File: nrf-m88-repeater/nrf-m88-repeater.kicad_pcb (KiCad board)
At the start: 2 copper layers, 14 parts, among them J1 Conn_02x03_Counter_Clockwise, SW1 SW_Push, U1 ATmega88-20P, U2 NRF24L01_Breakout, U3 LP2950-3.3_TO92

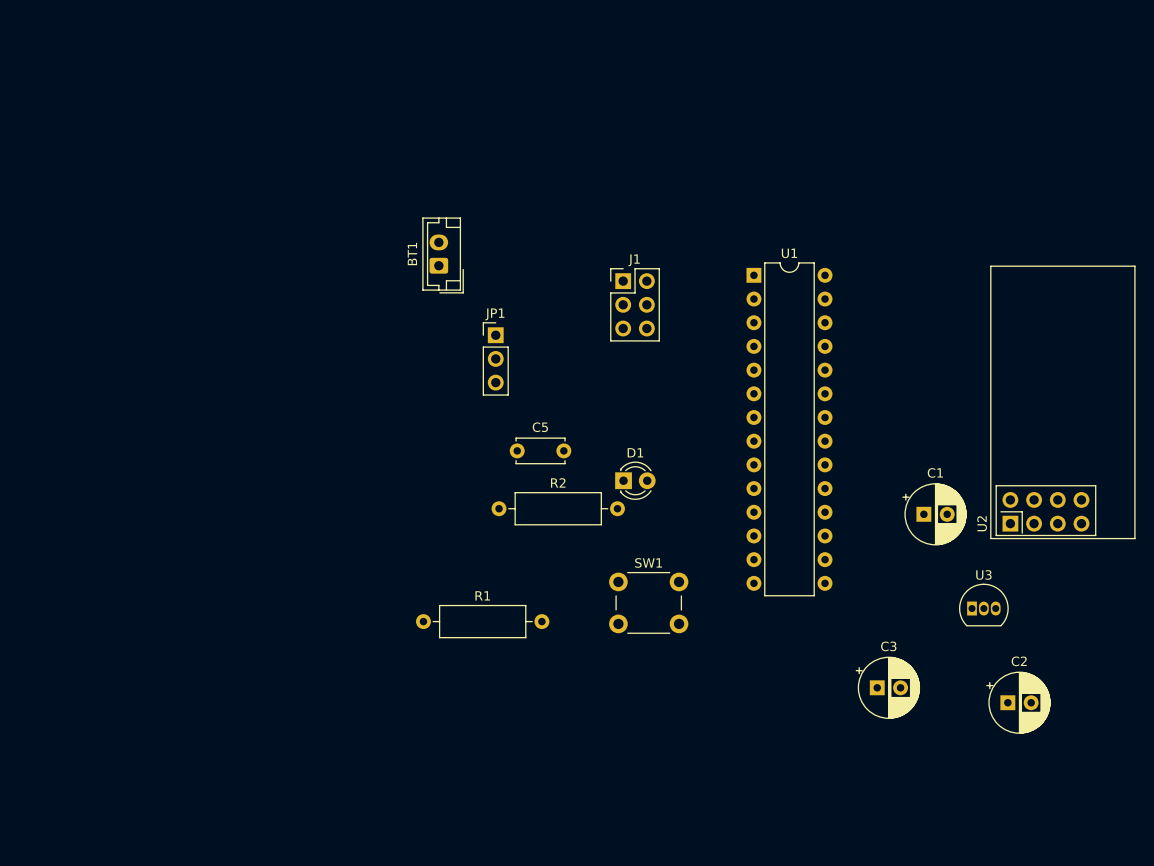
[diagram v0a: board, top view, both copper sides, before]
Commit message: Updated Generic KiCad Model
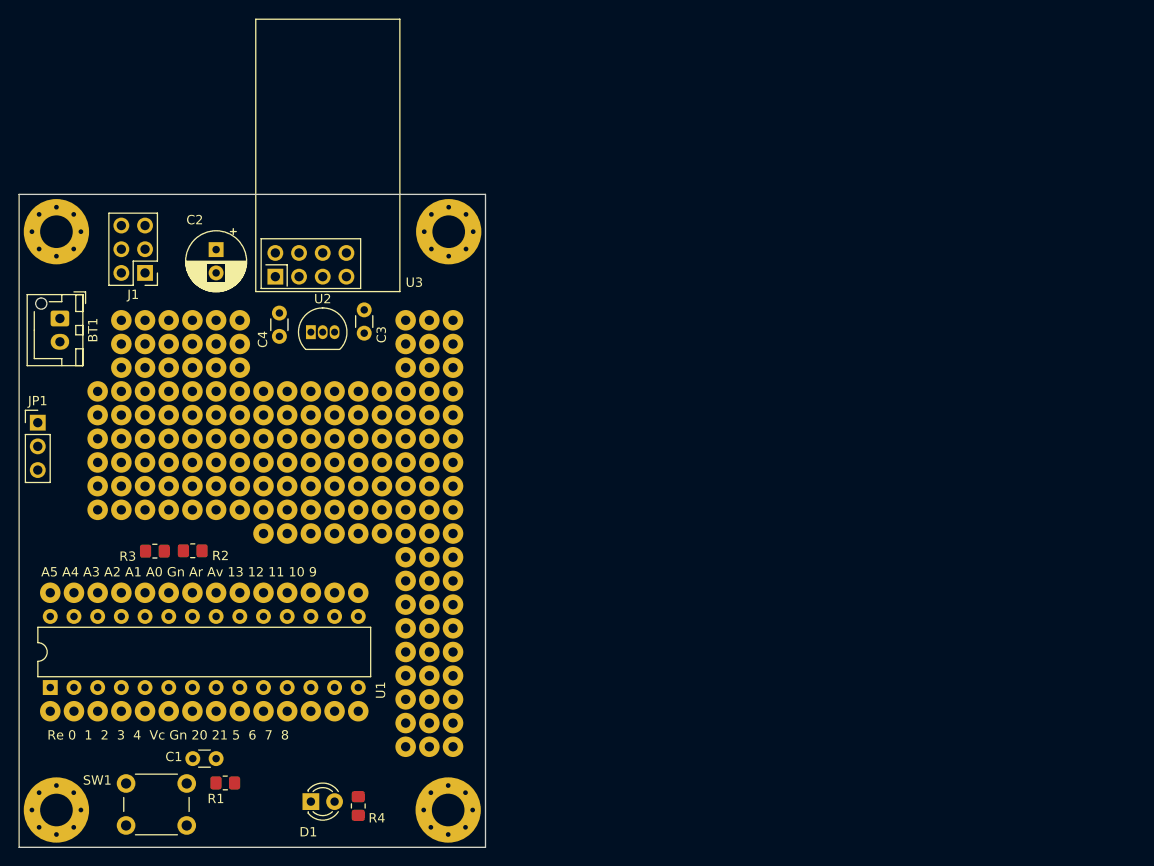
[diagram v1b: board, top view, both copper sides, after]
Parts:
- removed the C2 at (156.0, 104.5)
- removed C5: 100n, Capacitor_THT:C_Disc_D5.0mm_W2.5mm_P5.00mm
- added C1: 100n, Capacitor_THT:C_Disc_D3.0mm_W1.6mm_P2.50mm, F.Cu at (68.6, 110.5)
- added C3: 1u, Capacitor_THT:C_Disc_D3.0mm_W1.6mm_P2.50mm, F.Cu at (87.0, 62.4)
- added H1: MountingHole, MountingHole:MountingHole_3.5mm_Pad_Via, F.Cu at (96.1, 54.0)
- added H2: MountingHole, MountingHole:MountingHole_3.5mm_Pad_Via, F.Cu at (54.0, 54.0)
- added H3: MountingHole, MountingHole:MountingHole_3.5mm_Pad_Via, F.Cu at (96.0, 116.0)
- added H4: MountingHole, MountingHole:MountingHole_3.5mm_Pad_Via, F.Cu at (54.0, 116.0)
- added R2: 8.2k, Resistor_SMD:R_0805_2012Metric_Pad1.20x1.40mm_HandSolder, F.Cu at (68.6, 88.2)
- added R3: 2.2k, Resistor_SMD:R_0805_2012Metric_Pad1.20x1.40mm_HandSolder, F.Cu at (64.6, 88.2)
- added REF**: Pad, mikes-feet-library:ProtoPad, F.Cu at (58.4, 73.7)
- added REF**: Pad, mikes-feet-library:ProtoPad, F.Cu at (96.5, 66.0)
- added REF**: Pad, mikes-feet-library:ProtoPad, F.Cu at (91.4, 104.1)
- added REF**: Pad, mikes-feet-library:ProtoPad, F.Cu at (83.8, 76.2)
- added REF**: Pad, mikes-feet-library:ProtoPad, F.Cu at (76.2, 105.4)
- added REF**: Pad, mikes-feet-library:ProtoPad, F.Cu at (73.7, 105.4)
- added REF**: Pad, mikes-feet-library:ProtoPad, F.Cu at (96.5, 101.6)
- added REF**: Pad, mikes-feet-library:ProtoPad, F.Cu at (71.1, 83.8)
- added REF**: Pad, mikes-feet-library:ProtoPad, F.Cu at (73.7, 71.1)
- added REF**: Pad, mikes-feet-library:ProtoPad, F.Cu at (61.0, 92.7)
- added REF**: Pad, mikes-feet-library:ProtoPad, F.Cu at (81.3, 71.1)
- added REF**: Pad, mikes-feet-library:ProtoPad, F.Cu at (81.3, 78.7)
- added REF**: Pad, mikes-feet-library:ProtoPad, F.Cu at (58.4, 81.3)
- added REF**: Pad, mikes-feet-library:ProtoPad, F.Cu at (96.5, 86.4)
- added REF**: Pad, mikes-feet-library:ProtoPad, F.Cu at (61.0, 83.8)
- added REF**: Pad, mikes-feet-library:ProtoPad, F.Cu at (94.0, 66.0)
- added REF**: Pad, mikes-feet-library:ProtoPad, F.Cu at (63.5, 83.8)
- added REF**: Pad, mikes-feet-library:ProtoPad, F.Cu at (86.4, 92.7)
- added REF**: Pad, mikes-feet-library:ProtoPad, F.Cu at (61.0, 81.3)
- added REF**: Pad, mikes-feet-library:ProtoPad, F.Cu at (94.0, 73.7)
- added REF**: Pad, mikes-feet-library:ProtoPad, F.Cu at (73.7, 66.0)
- added REF**: Pad, mikes-feet-library:ProtoPad, F.Cu at (73.7, 68.6)
- added REF**: Pad, mikes-feet-library:ProtoPad, F.Cu at (58.4, 71.1)
- added REF**: Pad, mikes-feet-library:ProtoPad, F.Cu at (73.7, 78.7)
- added REF**: Pad, mikes-feet-library:ProtoPad, F.Cu at (66.0, 73.7)
- added REF**: Pad, mikes-feet-library:ProtoPad, F.Cu at (96.5, 88.9)
- added REF**: Pad, mikes-feet-library:ProtoPad, F.Cu at (91.4, 109.2)
- added REF**: Pad, mikes-feet-library:ProtoPad, F.Cu at (63.5, 78.7)
- added REF**: Pad, mikes-feet-library:ProtoPad, F.Cu at (88.9, 76.2)
- added REF**: Pad, mikes-feet-library:ProtoPad, F.Cu at (81.3, 83.8)
- added REF**: Pad, mikes-feet-library:ProtoPad, F.Cu at (58.4, 76.2)
- added REF**: Pad, mikes-feet-library:ProtoPad, F.Cu at (68.6, 78.7)
- added REF**: Pad, mikes-feet-library:ProtoPad, F.Cu at (94.0, 99.1)
- added REF**: Pad, mikes-feet-library:ProtoPad, F.Cu at (68.6, 66.0)
- added REF**: Pad, mikes-feet-library:ProtoPad, F.Cu at (83.8, 86.4)
- added REF**: Pad, mikes-feet-library:ProtoPad, F.Cu at (78.7, 76.2)
- added REF**: Pad, mikes-feet-library:ProtoPad, F.Cu at (73.7, 63.5)
- added REF**: Pad, mikes-feet-library:ProtoPad, F.Cu at (68.6, 73.7)
- added REF**: Pad, mikes-feet-library:ProtoPad, F.Cu at (63.5, 105.4)
- added REF**: Pad, mikes-feet-library:ProtoPad, F.Cu at (86.4, 81.3)
- added REF**: Pad, mikes-feet-library:ProtoPad, F.Cu at (66.0, 92.7)
- added REF**: Pad, mikes-feet-library:ProtoPad, F.Cu at (53.3, 92.7)
- added REF**: Pad, mikes-feet-library:ProtoPad, F.Cu at (94.0, 68.6)
- added REF**: Pad, mikes-feet-library:ProtoPad, F.Cu at (91.4, 86.4)
- added REF**: Pad, mikes-feet-library:ProtoPad, F.Cu at (96.5, 68.6)
- added REF**: Pad, mikes-feet-library:ProtoPad, F.Cu at (83.8, 105.4)
- added REF**: Pad, mikes-feet-library:ProtoPad, F.Cu at (76.2, 81.3)
- added REF**: Pad, mikes-feet-library:ProtoPad, F.Cu at (94.0, 101.6)
- added REF**: Pad, mikes-feet-library:ProtoPad, F.Cu at (86.4, 78.7)
- added REF**: Pad, mikes-feet-library:ProtoPad, F.Cu at (58.4, 83.8)
- added REF**: Pad, mikes-feet-library:ProtoPad, F.Cu at (55.9, 92.7)
- added REF**: Pad, mikes-feet-library:ProtoPad, F.Cu at (66.0, 63.5)
- added REF**: Pad, mikes-feet-library:ProtoPad, F.Cu at (76.2, 71.1)
- added REF**: Pad, mikes-feet-library:ProtoPad, F.Cu at (96.5, 73.7)
- added REF**: Pad, mikes-feet-library:ProtoPad, F.Cu at (83.8, 73.7)
- added REF**: Pad, mikes-feet-library:ProtoPad, F.Cu at (63.5, 66.0)
- added REF**: Pad, mikes-feet-library:ProtoPad, F.Cu at (96.5, 83.8)
- added REF**: Pad, mikes-feet-library:ProtoPad, F.Cu at (66.0, 66.0)
- added REF**: Pad, mikes-feet-library:ProtoPad, F.Cu at (78.7, 71.1)
- added REF**: Pad, mikes-feet-library:ProtoPad, F.Cu at (91.4, 99.1)
- added REF**: Pad, mikes-feet-library:ProtoPad, F.Cu at (68.6, 92.7)
- added REF**: Pad, mikes-feet-library:ProtoPad, F.Cu at (81.3, 76.2)
- added REF**: Pad, mikes-feet-library:ProtoPad, F.Cu at (66.0, 78.7)
- added REF**: Pad, mikes-feet-library:ProtoPad, F.Cu at (83.8, 71.1)
- added REF**: Pad, mikes-feet-library:ProtoPad, F.Cu at (61.0, 71.1)
- added REF**: Pad, mikes-feet-library:ProtoPad, F.Cu at (61.0, 63.5)
- added REF**: Pad, mikes-feet-library:ProtoPad, F.Cu at (78.7, 73.7)
- added REF**: Pad, mikes-feet-library:ProtoPad, F.Cu at (61.0, 68.6)
- added REF**: Pad, mikes-feet-library:ProtoPad, F.Cu at (91.4, 66.0)
- added REF**: Pad, mikes-feet-library:ProtoPad, F.Cu at (66.0, 81.3)
- added REF**: Pad, mikes-feet-library:ProtoPad, F.Cu at (61.0, 76.2)
- added REF**: Pad, mikes-feet-library:ProtoPad, F.Cu at (83.8, 92.7)
- added REF**: Pad, mikes-feet-library:ProtoPad, F.Cu at (81.3, 73.7)
- added REF**: Pad, mikes-feet-library:ProtoPad, F.Cu at (94.0, 71.1)
- added REF**: Pad, mikes-feet-library:ProtoPad, F.Cu at (76.2, 78.7)
- added REF**: Pad, mikes-feet-library:ProtoPad, F.Cu at (96.5, 81.3)
- added REF**: Pad, mikes-feet-library:ProtoPad, F.Cu at (88.9, 73.7)
- added REF**: Pad, mikes-feet-library:ProtoPad, F.Cu at (81.3, 92.7)
- added REF**: Pad, mikes-feet-library:ProtoPad, F.Cu at (53.3, 105.4)
- added REF**: Pad, mikes-feet-library:ProtoPad, F.Cu at (94.0, 86.4)
- added REF**: Pad, mikes-feet-library:ProtoPad, F.Cu at (66.0, 83.8)
- added REF**: Pad, mikes-feet-library:ProtoPad, F.Cu at (96.5, 94.0)
- added REF**: Pad, mikes-feet-library:ProtoPad, F.Cu at (58.4, 92.7)
- added REF**: Pad, mikes-feet-library:ProtoPad, F.Cu at (78.7, 83.8)
- added REF**: Pad, mikes-feet-library:ProtoPad, F.Cu at (96.5, 76.2)
- added REF**: Pad, mikes-feet-library:ProtoPad, F.Cu at (94.0, 83.8)
- added REF**: Pad, mikes-feet-library:ProtoPad, F.Cu at (76.2, 83.8)
- added REF**: Pad, mikes-feet-library:ProtoPad, F.Cu at (68.6, 83.8)
- added REF**: Pad, mikes-feet-library:ProtoPad, F.Cu at (81.3, 81.3)
- added REF**: Pad, mikes-feet-library:ProtoPad, F.Cu at (58.4, 105.4)
- added REF**: Pad, mikes-feet-library:ProtoPad, F.Cu at (91.4, 73.7)
- added REF**: Pad, mikes-feet-library:ProtoPad, F.Cu at (83.8, 83.8)
- added REF**: Pad, mikes-feet-library:ProtoPad, F.Cu at (68.6, 63.5)
- added REF**: Pad, mikes-feet-library:ProtoPad, F.Cu at (86.4, 71.1)
- added REF**: Pad, mikes-feet-library:ProtoPad, F.Cu at (78.7, 105.4)
- added REF**: Pad, mikes-feet-library:ProtoPad, F.Cu at (76.2, 86.4)
- added REF**: Pad, mikes-feet-library:ProtoPad, F.Cu at (96.5, 106.7)
- added REF**: Pad, mikes-feet-library:ProtoPad, F.Cu at (88.9, 78.7)
- added REF**: Pad, mikes-feet-library:ProtoPad, F.Cu at (83.8, 81.3)
- added REF**: Pad, mikes-feet-library:ProtoPad, F.Cu at (88.9, 83.8)
- added REF**: Pad, mikes-feet-library:ProtoPad, F.Cu at (76.2, 92.7)
- added REF**: Pad, mikes-feet-library:ProtoPad, F.Cu at (71.1, 78.7)
- added REF**: Pad, mikes-feet-library:ProtoPad, F.Cu at (91.4, 91.4)
- added REF**: Pad, mikes-feet-library:ProtoPad, F.Cu at (63.5, 76.2)
- added REF**: Pad, mikes-feet-library:ProtoPad, F.Cu at (81.3, 105.4)
- added REF**: Pad, mikes-feet-library:ProtoPad, F.Cu at (63.5, 68.6)
- added REF**: Pad, mikes-feet-library:ProtoPad, F.Cu at (71.1, 68.6)
- added REF**: Pad, mikes-feet-library:ProtoPad, F.Cu at (94.0, 88.9)
- added REF**: Pad, mikes-feet-library:ProtoPad, F.Cu at (96.5, 71.1)
- added REF**: Pad, mikes-feet-library:ProtoPad, F.Cu at (91.4, 83.8)
- added REF**: Pad, mikes-feet-library:ProtoPad, F.Cu at (78.7, 92.7)
- added REF**: Pad, mikes-feet-library:ProtoPad, F.Cu at (86.4, 73.7)
- added REF**: Pad, mikes-feet-library:ProtoPad, F.Cu at (71.1, 63.5)
- added REF**: Pad, mikes-feet-library:ProtoPad, F.Cu at (96.5, 104.1)
- added REF**: Pad, mikes-feet-library:ProtoPad, F.Cu at (88.9, 71.1)
- added REF**: Pad, mikes-feet-library:ProtoPad, F.Cu at (83.8, 78.7)
- added REF**: Pad, mikes-feet-library:ProtoPad, F.Cu at (76.2, 76.2)
- added REF**: Pad, mikes-feet-library:ProtoPad, F.Cu at (61.0, 73.7)
- added REF**: Pad, mikes-feet-library:ProtoPad, F.Cu at (96.5, 91.4)
- added REF**: Pad, mikes-feet-library:ProtoPad, F.Cu at (94.0, 76.2)
- added REF**: Pad, mikes-feet-library:ProtoPad, F.Cu at (94.0, 109.2)
- added REF**: Pad, mikes-feet-library:ProtoPad, F.Cu at (96.5, 99.1)
- added REF**: Pad, mikes-feet-library:ProtoPad, F.Cu at (88.9, 81.3)
- added REF**: Pad, mikes-feet-library:ProtoPad, F.Cu at (63.5, 92.7)
- added REF**: Pad, mikes-feet-library:ProtoPad, F.Cu at (63.5, 81.3)
- added REF**: Pad, mikes-feet-library:ProtoPad, F.Cu at (86.4, 86.4)
- added REF**: Pad, mikes-feet-library:ProtoPad, F.Cu at (94.0, 91.4)
- added REF**: Pad, mikes-feet-library:ProtoPad, F.Cu at (91.4, 101.6)
- added REF**: Pad, mikes-feet-library:ProtoPad, F.Cu at (63.5, 73.7)
- added REF**: Pad, mikes-feet-library:ProtoPad, F.Cu at (66.0, 68.6)
- added REF**: Pad, mikes-feet-library:ProtoPad, F.Cu at (94.0, 106.7)
- added REF**: Pad, mikes-feet-library:ProtoPad, F.Cu at (61.0, 66.0)
- added REF**: Pad, mikes-feet-library:ProtoPad, F.Cu at (78.7, 78.7)
- added REF**: Pad, mikes-feet-library:ProtoPad, F.Cu at (91.4, 63.5)
- added REF**: Pad, mikes-feet-library:ProtoPad, F.Cu at (78.7, 81.3)
- added REF**: Pad, mikes-feet-library:ProtoPad, F.Cu at (94.0, 78.7)
- added REF**: Pad, mikes-feet-library:ProtoPad, F.Cu at (73.7, 92.7)
- added REF**: Pad, mikes-feet-library:ProtoPad, F.Cu at (63.5, 71.1)
- added REF**: Pad, mikes-feet-library:ProtoPad, F.Cu at (91.4, 71.1)
- added REF**: Pad, mikes-feet-library:ProtoPad, F.Cu at (66.0, 105.4)
- added REF**: Pad, mikes-feet-library:ProtoPad, F.Cu at (91.4, 78.7)
- added REF**: Pad, mikes-feet-library:ProtoPad, F.Cu at (71.1, 71.1)
- added REF**: Pad, mikes-feet-library:ProtoPad, F.Cu at (68.6, 105.4)
- added REF**: Pad, mikes-feet-library:ProtoPad, F.Cu at (63.5, 63.5)
- added REF**: Pad, mikes-feet-library:ProtoPad, F.Cu at (66.0, 76.2)
- added REF**: Pad, mikes-feet-library:ProtoPad, F.Cu at (86.4, 83.8)
- added REF**: Pad, mikes-feet-library:ProtoPad, F.Cu at (68.6, 81.3)
- added REF**: Pad, mikes-feet-library:ProtoPad, F.Cu at (91.4, 76.2)
- added REF**: Pad, mikes-feet-library:ProtoPad, F.Cu at (94.0, 94.0)
- added REF**: Pad, mikes-feet-library:ProtoPad, F.Cu at (81.3, 86.4)
- added REF**: Pad, mikes-feet-library:ProtoPad, F.Cu at (61.0, 105.4)
- added REF**: Pad, mikes-feet-library:ProtoPad, F.Cu at (91.4, 88.9)
- added REF**: Pad, mikes-feet-library:ProtoPad, F.Cu at (76.2, 73.7)
- added REF**: Pad, mikes-feet-library:ProtoPad, F.Cu at (73.7, 76.2)
- added REF**: Pad, mikes-feet-library:ProtoPad, F.Cu at (91.4, 106.7)
- added REF**: Pad, mikes-feet-library:ProtoPad, F.Cu at (71.1, 92.7)
- added REF**: Pad, mikes-feet-library:ProtoPad, F.Cu at (71.1, 105.4)
- added REF**: Pad, mikes-feet-library:ProtoPad, F.Cu at (58.4, 78.7)
- added REF**: Pad, mikes-feet-library:ProtoPad, F.Cu at (94.0, 104.1)
- added REF**: Pad, mikes-feet-library:ProtoPad, F.Cu at (96.5, 96.5)
- added REF**: Pad, mikes-feet-library:ProtoPad, F.Cu at (91.4, 81.3)
- added REF**: Pad, mikes-feet-library:ProtoPad, F.Cu at (78.7, 86.4)
- added REF**: Pad, mikes-feet-library:ProtoPad, F.Cu at (71.1, 66.0)
- added REF**: Pad, mikes-feet-library:ProtoPad, F.Cu at (96.5, 63.5)
- added REF**: Pad, mikes-feet-library:ProtoPad, F.Cu at (71.1, 81.3)
- added REF**: Pad, mikes-feet-library:ProtoPad, F.Cu at (73.7, 81.3)
- added REF**: Pad, mikes-feet-library:ProtoPad, F.Cu at (86.4, 76.2)
- added REF**: Pad, mikes-feet-library:ProtoPad, F.Cu at (94.0, 81.3)
- added REF**: Pad, mikes-feet-library:ProtoPad, F.Cu at (61.0, 78.7)
- added REF**: Pad, mikes-feet-library:ProtoPad, F.Cu at (73.7, 73.7)
- added REF**: Pad, mikes-feet-library:ProtoPad, F.Cu at (55.9, 105.4)
- added REF**: Pad, mikes-feet-library:ProtoPad, F.Cu at (68.6, 76.2)
- added REF**: Pad, mikes-feet-library:ProtoPad, F.Cu at (71.1, 76.2)
- added REF**: Pad, mikes-feet-library:ProtoPad, F.Cu at (91.4, 68.6)
- added REF**: Pad, mikes-feet-library:ProtoPad, F.Cu at (68.6, 68.6)
- added REF**: Pad, mikes-feet-library:ProtoPad, F.Cu at (94.0, 63.5)
- added REF**: Pad, mikes-feet-library:ProtoPad, F.Cu at (88.9, 86.4)
- added REF**: Pad, mikes-feet-library:ProtoPad, F.Cu at (86.4, 105.4)
- added REF**: Pad, mikes-feet-library:ProtoPad, F.Cu at (68.6, 71.1)
- added REF**: Pad, mikes-feet-library:ProtoPad, F.Cu at (94.0, 96.5)
- added REF**: Pad, mikes-feet-library:ProtoPad, F.Cu at (96.5, 78.7)
- added REF**: Pad, mikes-feet-library:ProtoPad, F.Cu at (96.5, 109.2)
- added REF**: Pad, mikes-feet-library:ProtoPad, F.Cu at (71.1, 73.7)
- added REF**: Pad, mikes-feet-library:ProtoPad, F.Cu at (73.7, 83.8)
- added REF**: Pad, mikes-feet-library:ProtoPad, F.Cu at (66.0, 71.1)
- added REF**: Pad, mikes-feet-library:ProtoPad, F.Cu at (91.4, 96.5)
- added REF**: Pad, mikes-feet-library:ProtoPad, F.Cu at (91.4, 94.0)
- BT1: value Battery -> 18650 Battery Holder; footprint Connector_JST:JST_EH_B2B-EH-A_1x02_P2.50mm_Vertical -> Connector_JST:JST_XH_B2B-XH-AM_1x02_P2.50mm_Vertical
- C4: renamed from C3; footprint Capacitor_THT:CP_Radial_D6.3mm_P2.50mm -> Capacitor_THT:C_Disc_D3.0mm_W1.6mm_P2.50mm
- JP1: value Jumper_3_Bridged12 -> PWR Sel.
- R1: footprint Resistor_THT:R_Axial_DIN0309_L9.0mm_D3.2mm_P12.70mm_Horizontal -> Resistor_SMD:R_0805_2012Metric_Pad1.20x1.40mm_HandSolder
- R4: renamed from R2; footprint Resistor_THT:R_Axial_DIN0309_L9.0mm_D3.2mm_P12.70mm_Horizontal -> Resistor_SMD:R_0805_2012Metric_Pad1.20x1.40mm_HandSolder
- SW1: value SW_Push -> RESET
- U1: value ATmega88-20P -> ATmega88
- U2: renamed from U3; value LP2950-3.3_TO92 -> LP2950-3.3
- moved U1 87.4 mm to (53.3, 102.9), turned to 90 degrees
- moved U3 83.1 mm to (77.5, 58.8)
- moved C2 81.0 mm to (71.1, 55.9), turned to -90 degrees
- moved U2 76.8 mm to (81.3, 64.8)
- moved C4 75.6 mm to (77.9, 62.7), turned to -90 degrees
- moved SW1 53.1 mm to (68.0, 117.7), turned to 180 degrees
- moved J1 51.3 mm to (63.5, 58.4), turned to 180 degrees
- moved JP1 50.0 mm to (52.0, 74.5)
- moved D1 48.0 mm to (81.3, 115.1)
- moved BT1 41.0 mm to (54.4, 63.3), turned to -90 degrees
- moved R4 35.3 mm to (86.4, 115.6), turned to -90 degrees
- moved R1 27.4 mm to (72.1, 113.1), turned to 180 degrees
- renumbered C1 to C2, U2 to U3
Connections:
- net /ACT renamed /D8ACT
- net /MISO renamed /D12MISO
- net /MOSI renamed /D11MOSI
- net /SCK renamed /D13SCK
- C4 pad 1: /3.3V -> GND
- C4 pad 2: GND -> /3.3V
- JP1 pad 2: Net-(JP1-C) -> /VCC
- R1 pad 1: /RESET -> GND
- R1 pad 2: Net-(JP1-C) -> Net-(R1-Pad2)
- SW1 pad 1: GND -> /RESET
- SW1 pad 2: Net-(JP1-C) -> Net-(R1-Pad2)
- U1 pad 10: unconnected-(U1-XTAL2/PB7-Pad10) -> /D21X2
- U1 pad 11: unconnected-(U1-PD5-Pad11) -> /D5
- U1 pad 12: unconnected-(U1-PD6-Pad12) -> /D6
- U1 pad 13: unconnected-(U1-PD7-Pad13) -> /D7
- U1 pad 15: /CSN -> /D9
- U1 pad 16: /CE -> /D10
- U1 pad 2: unconnected-(U1-PD0-Pad2) -> /D0RX
- U1 pad 20: Net-(JP1-C) -> /VCC
- U1 pad 23: unconnected-(U1-PC0-Pad23) -> /D14A0
- U1 pad 24: unconnected-(U1-PC1-Pad24) -> /D15A1
- U1 pad 25: unconnected-(U1-PC2-Pad25) -> /D16A2
- U1 pad 26: unconnected-(U1-PC3-Pad26) -> /D17A3
- U1 pad 27: unconnected-(U1-PC4-Pad27) -> /D18A4
- U1 pad 28: unconnected-(U1-PC5-Pad28) -> /D19A5
- U1 pad 3: unconnected-(U1-PD1-Pad3) -> /D1TX
- U1 pad 4: unconnected-(U1-PD2-Pad4) -> /D2
- U1 pad 5: unconnected-(U1-PD3-Pad5) -> /D3
- U1 pad 6: unconnected-(U1-PD4-Pad6) -> /D4
- U1 pad 7: Net-(JP1-C) -> /VCC
- U1 pad 9: unconnected-(U1-XTAL1/PB6-Pad9) -> /D20X1
- U2 pad 3: Net-(JP1-C) -> /VCC
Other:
- board outline added: 50 x 70 mm
- board text added: "A5 A4 A3 A2 A1 A0 Gn Ar Av 13 12 11 10 9"
- board text added: "Re 0 1 2 3 4 Vc Gn 20 21 5 6 7 8"
